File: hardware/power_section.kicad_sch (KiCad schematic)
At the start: 40 parts, among them J2 Conn_01x02, J3 USB_C_Receptacle_USB2.0_16P, U2 SW_SPDT_3pin, U3 HX3242, U4 TP4056, U5 FS8502A, U6 DW01A, U7 MIC5504-3.3YM5

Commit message: Second revision of schematic
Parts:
- removed U7: MIC5504-3.3YM5, Package_TO_SOT_SMD:SOT-23-5, symbol Regulator_Linear:MIC5504-3.3YM5
- added D4: 1N4148, Diode_THT:D_DO-35_SOD27_P7.62mm_Horizontal, symbol Diode:1N4148
- added R18: 1k, Resistor_SMD:R_0603_1608Metric, symbol Device:R
- added SW1: SW_Push, Button_Switch_SMD:SW_SPST_TL3342, symbol Switch:SW_Push
- added U7: AP2112K-3.3, Package_TO_SOT_SMD:SOT-23-5, symbol Regulator_Linear:AP2112K-3.3
- C3, C5: footprint Capacitor_THT:CP_Radial_D4.0mm_P1.50mm -> Capacitor_SMD:CP_Elec_6.3x3
- R10: renamed from R9; footprint (none) -> Resistor_SMD:R_0603_1608Metric
- R17: renamed from R16; value 0 -> 1k
- R20: renamed from R17; value 0 -> 1k
- R21: renamed from R18; value 1k -> 10k
- R9: renamed from R8; footprint (none) -> Resistor_SMD:R_0603_1608Metric
- renumbered R10 to R11, R11 to R12, R12 to R13, R13 to R14, R14 to R15, R15 to R16, R20 to R22, R21 to R23, R6 to R7, R7 to R8
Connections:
- net Ubatt is gone; now on net +BATT: R10.1, R9.2
- net +3V3: now also U7.5 (VOUT)
- net +5V: now also U7.1 (VIN)
- net +VSW: now also SW1.1
- net GND: now also U7.2 (GND)
- net POWER_EN: now also D4.2 (A); no longer R17.1, R20.2, R21.1
- net at D3.2 (A), L1.2, U3.1 (SW)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: now also U3.9 (SW)
- net at R20.1, R22.1: now also U7.3 (EN)
- new net: D4.1 (K), R17.1, R18.1, R20.2, R21.1
- new net: R18.2, SW1.2
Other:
- moved on the sheet: C11, R16, R17, R20, R21, R22, R23

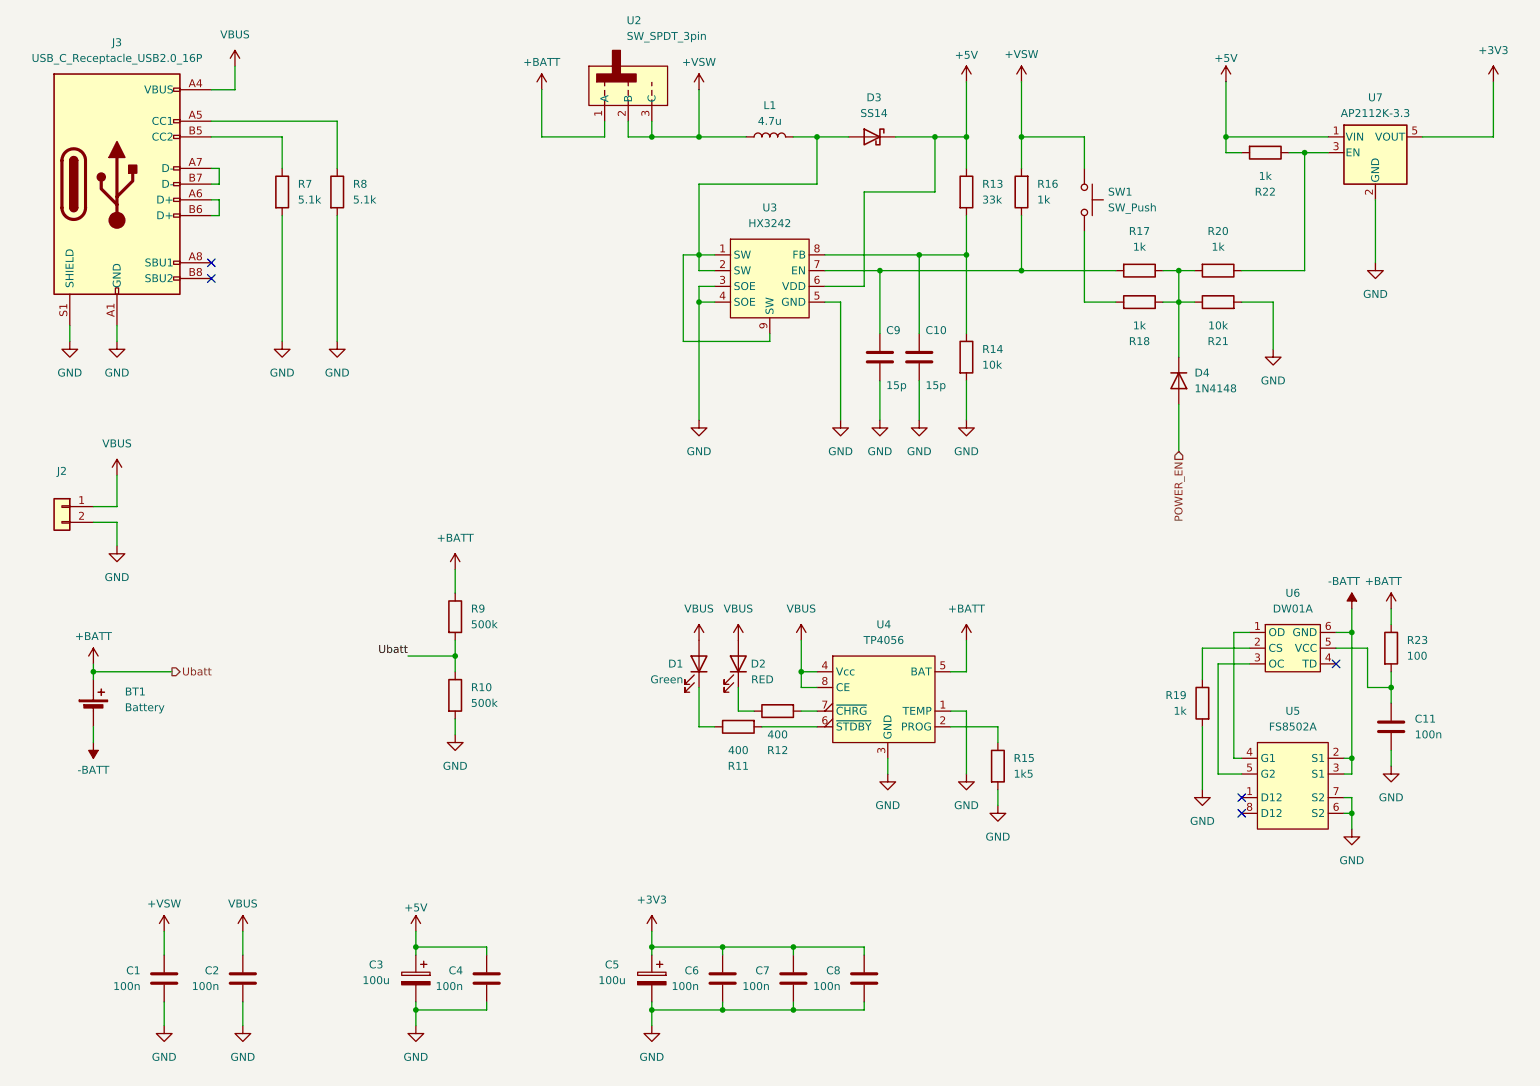
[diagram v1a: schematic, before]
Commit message: Initial PCB placement and some schematic changes
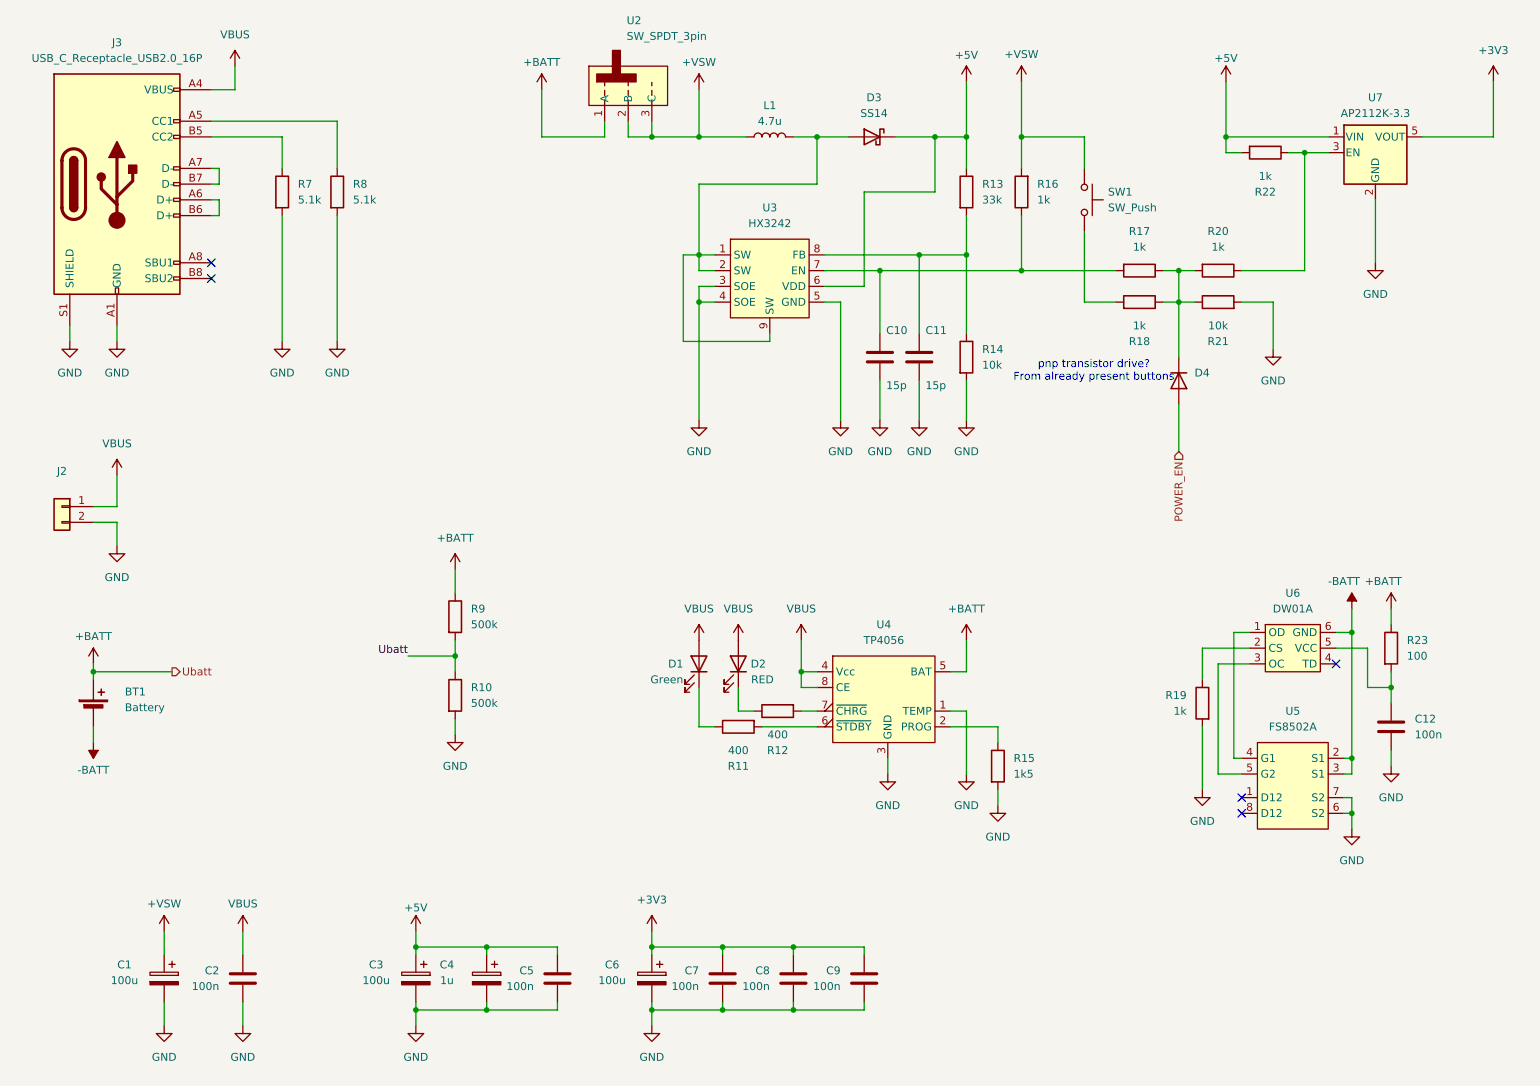
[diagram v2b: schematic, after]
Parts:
- removed C1: 100n, Capacitor_SMD:C_0603_1608Metric, symbol Device:C
- removed D4: 1N4148, Diode_THT:D_DO-35_SOD27_P7.62mm_Horizontal, symbol Diode:1N4148
- added C1: 100u, Capacitor_SMD:CP_Elec_6.3x3, symbol Device:C_Polarized
- added C4: 1u, Capacitor_SMD:CP_Elec_6.3x3, symbol Device:C_Polarized
- added D4: D, Diode_SMD:D_0805_2012Metric, symbol Device:D
- D1, D2: footprint Diode_SMD:D_0805_2012Metric -> Diode_SMD:D_0603_1608Metric_Pad1.05x0.95mm_HandSolder
- D3: footprint Diode_SMD:D_SMB -> Diode_SMD:D_SMA
- renumbered C9 to C10, C10 to C11, C11 to C12, C4 to C5, C5 to C6, C6 to C7, C7 to C8, C8 to C9
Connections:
- net +5V: now also C4.1
- net +VSW: now also C1.1
- net GND: now also C1.2, C4.2
- net POWER_EN: now also D4.2 (A)
- net at R17.1, R18.1, R20.2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: now also D4.1 (K)
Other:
- note added: "pnp transistor drive? From already present buttons"
- moved on the sheet: C5

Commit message: Audio improvements
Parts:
- removed C4: 1u, Capacitor_SMD:CP_Elec_6.3x3, symbol Device:C_Polarized
- renumbered C11 to C10, C12 to C11, C5 to C4, C6 to C5, C7 to C6, C8 to C7, C9 to C8, C10 to C9
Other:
- moved on the sheet: C4
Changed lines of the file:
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@@
 	)
 	(junction
-		(at 102.87 181.61)
-		(diameter 0)
-		(color 0 0 0 0)
-	)
-	(junction
 		(at 189.23 40.64)
 		(diameter 0)
@@
 	)
 	(junction
-		(at 102.87 171.45)
-		(diameter 0)
-		(color 0 0 0 0)
-	)
-	(junction
 		(at 39.37 127)
 		(diameter 0)
@@
 	(wire
 		(pts
-			(xy 102.87 180.34) (xy 102.87 181.61)
-		)
-		(stroke
-			(width 0)
-			(type default)
-		)
-	)
-	(wire
-		(pts
 			(xy 222.25 40.64) (xy 222.25 43.18)
 		)
@@
 	(wire
 		(pts
-			(xy 114.3 171.45) (xy 102.87 171.45)
-		)
-		(stroke
-			(width 0)
-			(type default)
-		)
-	)
-	(wire
-		(pts
 			(xy 156.21 48.26) (xy 156.21 40.64)
 		)
@@
 	(wire
 		(pts
-			(xy 114.3 180.34) (xy 114.3 181.61)
+			(xy 104.14 180.34) (xy 104.14 181.61)
 		)
 		(stroke
@@
 	(wire
 		(pts
-			(xy 114.3 181.61) (xy 102.87 181.61)
+			(xy 91.44 181.61) (xy 104.14 181.61)
 		)
 		(stroke
@@
 	(wire
 		(pts
-			(xy 102.87 171.45) (xy 91.44 171.45)
+			(xy 91.44 171.45) (xy 104.14 171.45)
 		)
 		(stroke
@@
 	(wire
 		(pts
-			(xy 102.87 171.45) (xy 102.87 172.72)
-		)
-		(stroke
-			(width 0)
-			(type default)
-		)
-	)
-	(wire
-		(pts
 			(xy 199.39 67.31) (xy 204.47 67.31)
 		)
@@
 	(wire
 		(pts
-			(xy 102.87 181.61) (xy 91.44 181.61)
-		)
-		(stroke
-			(width 0)
-			(type default)
-		)
-	)
-	(wire
-		(pts
 			(xy 147.32 135.89) (xy 156.21 135.89)
 		)
@@
 	(wire
 		(pts
-			(xy 114.3 172.72) (xy 114.3 171.45)
+			(xy 104.14 172.72) (xy 104.14 171.45)
 		)
 		(stroke
@@
 		(on_board yes)
 		(dnp no)
-		(property "Reference" "C6"
+		(property "Reference" "C5"
 			(at 123.1265 174.3075 0)
 			(effects
@@
 			(project "esp8266_pygame"
 				(path "/fc3c54fb-6d1c-4231-9293-8fcb9c0b9706/b1f9fade-b7ed-42bb-82ec-b3a822ff35a4"
-					(reference "C6")
+					(reference "C5")
 					(unit 1)
 				)
@@
 		(on_board yes)
 		(dnp no)
-		(property "Reference" "C11"
+		(property "Reference" "C10"
 			(at 173.736 71.882 0)
 			(effects
@@
 			(project "esp8266_pygame"
 				(path "/fc3c54fb-6d1c-4231-9293-8fcb9c0b9706/b1f9fade-b7ed-42bb-82ec-b3a822ff35a4"
-					(reference "C11")
+					(reference "C10")
 					(unit 1)
 				)
@@
 		(on_board yes)
 		(dnp no)
-		(property "Reference" "C7"
+		(property "Reference" "C6"
 			(at 137.16 175.26 0)
 			(effects
@@
 			(project "esp8266_pygame"
 				(path "/fc3c54fb-6d1c-4231-9293-8fcb9c0b9706/b1f9fade-b7ed-42bb-82ec-b3a822ff35a4"
-					(reference "C7")
+					(reference "C6")
 					(unit 1)
 				)
@@
 		(on_board yes)
 		(dnp no)
-		(property "Reference" "C9"
+		(property "Reference" "C8"
 			(at 160.02 175.26 0)
 			(effects
@@
 			(project "esp8266_pygame"
 				(path "/fc3c54fb-6d1c-4231-9293-8fcb9c0b9706/b1f9fade-b7ed-42bb-82ec-b3a822ff35a4"
-					(reference "C9")
+					(reference "C8")
 					(unit 1)
 				)
@@
 		(on_board yes)
 		(dnp no)
-		(property "Reference" "C10"
+		(property "Reference" "C9"
 			(at 167.386 71.882 0)
 			(effects
@@
 			(project "esp8266_pygame"
 				(path "/fc3c54fb-6d1c-4231-9293-8fcb9c0b9706/b1f9fade-b7ed-42bb-82ec-b3a822ff35a4"
-					(reference "C10")
+					(reference "C9")
 					(unit 1)
 				)
@@
 	)
 	(symbol
-		(lib_id "Device:C_Polarized")
-		(at 102.87 176.53 0)
-		(mirror y)
-		(unit 1)
-		(exclude_from_sim no)
-		(in_bom yes)
-		(on_board yes)
-		(dnp no)
-		(property "Reference" "C4"
-			(at 96.4565 174.3075 0)
-			(effects
-				(font
-					(size 1.27 1.27)
-				)
-			)
-		)
-		(property "Value" "1u"
-			(at 96.4565 176.8475 0)
-			(effects
-				(font
-					(size 1.27 1.27)
-				)
-			)
-		)
-		(property "Footprint" "Capacitor_SMD:CP_Elec_6.3x3"
-			(at 101.9048 180.34 0)
-			(effects
-				(font
-					(size 1.27 1.27)
-				)
-				(hide yes)
-			)
-		)
-		(property "Datasheet" "~"
-			(at 102.87 176.53 0)
-			(effects
-				(font
-					(size 1.27 1.27)
-				)
-				(hide yes)
-			)
-		)
-		(property "Description" ""
-			(at 102.87 176.53 0)
-			(effects
-				(font
-					(size 1.27 1.27)
-				)
-			)
-		)
-		(pin "1"
-		)
-		(pin "2"
-		)
-		(instances
-			(project "esp8266_pygame"
-				(path "/fc3c54fb-6d1c-4231-9293-8fcb9c0b9706/b1f9fade-b7ed-42bb-82ec-b3a822ff35a4"
-					(reference "C4")
-					(unit 1)
-				)
-			)
-		)
-	)
-	(symbol
 		(lib_id "power:+BATT")
 		(at 111.76 33.02 0)
@@
 		(dnp no)
 		(fields_autoplaced yes)
-		(property "Reference" "C12"
+		(property "Reference" "C11"
 			(at 252.73 134.62 0)
 			(effects
@@
 			(project "esp8266_pygame"
 				(path "/fc3c54fb-6d1c-4231-9293-8fcb9c0b9706/b1f9fade-b7ed-42bb-82ec-b3a822ff35a4"
-					(reference "C12")
+					(reference "C11")
 					(unit 1)
 				)
@@
 		(on_board yes)
 		(dnp no)
-		(property "Reference" "C8"
+		(property "Reference" "C7"
 			(at 148.59 175.26 0)
 			(effects
@@
 			(project "esp8266_pygame"
 				(path "/fc3c54fb-6d1c-4231-9293-8fcb9c0b9706/b1f9fade-b7ed-42bb-82ec-b3a822ff35a4"
-					(reference "C8")
+					(reference "C7")
 					(unit 1)
 				)
@@
 	(symbol
 		(lib_id "Device:C")
-		(at 114.3 176.53 0)
+		(at 104.14 176.53 0)
 		(mirror x)
 		(unit 1)
@@
 		(on_board yes)
 		(dnp no)
-		(property "Reference" "C5"
-			(at 110.49 175.26 0)
+		(property "Reference" "C4"
+			(at 100.33 175.26 0)
 			(effects
 				(font
@@
 		)
 		(property "Value" "100n"
-			(at 110.49 177.8 0)
+			(at 100.33 177.8 0)
 			(effects
 				(font
@@
 		)
 		(property "Footprint" "Capacitor_SMD:C_0603_1608Metric"
-			(at 115.2652 172.72 0)
+			(at 105.1052 172.72 0)
 			(effects
 				(font
@@
 		)
 		(property "Datasheet" "~"
-			(at 114.3 176.53 0)
+			(at 104.14 176.53 0)
 			(effects
 				(font
@@
 		)
 		(property "Description" ""
-			(at 114.3 176.53 0)
+			(at 104.14 176.53 0)
 			(effects
 				(font
@@
 			(project "esp8266_pygame"
 				(path "/fc3c54fb-6d1c-4231-9293-8fcb9c0b9706/b1f9fade-b7ed-42bb-82ec-b3a822ff35a4"
-					(reference "C5")
+					(reference "C4")
 					(unit 1)
 				)

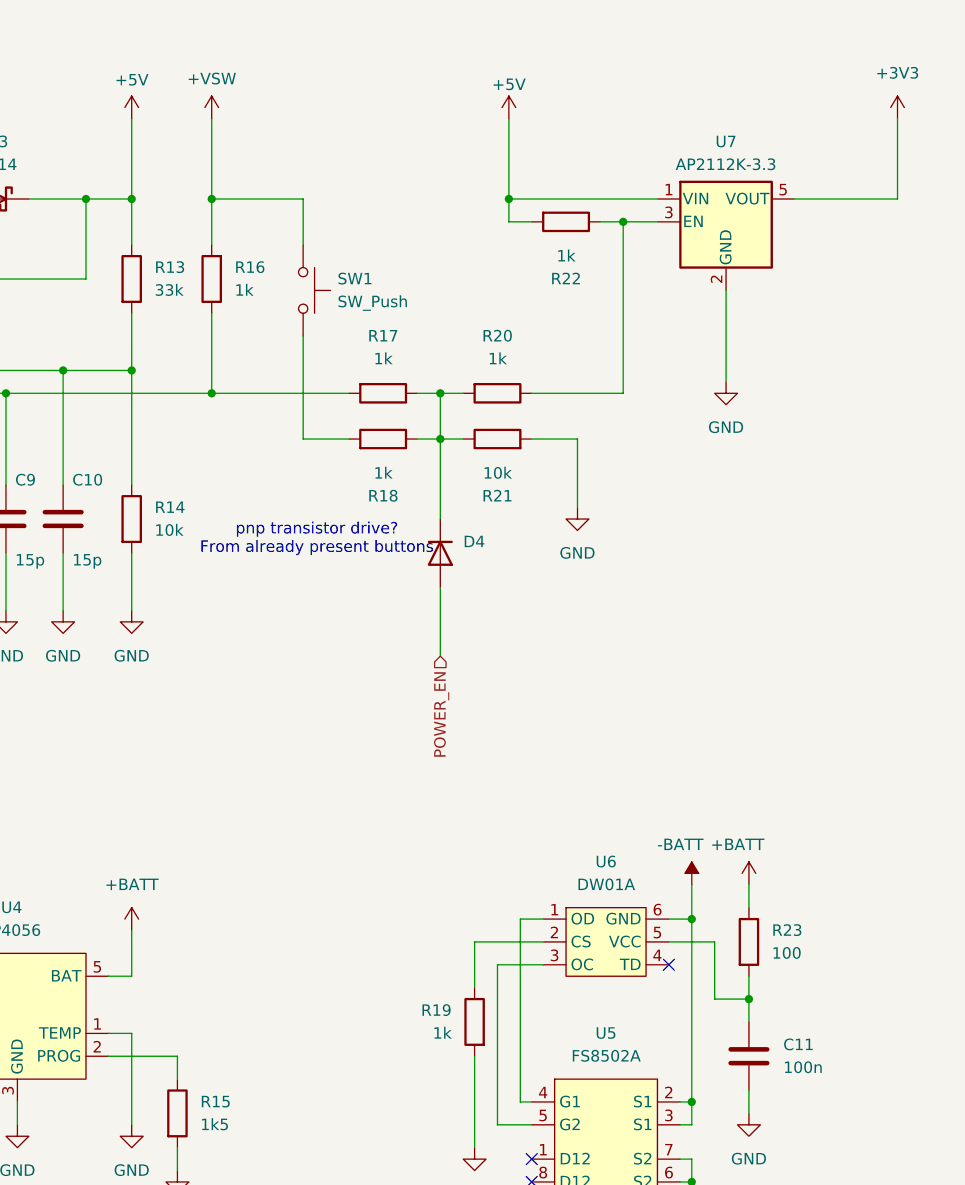
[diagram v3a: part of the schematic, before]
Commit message: Fixed power enable bypass
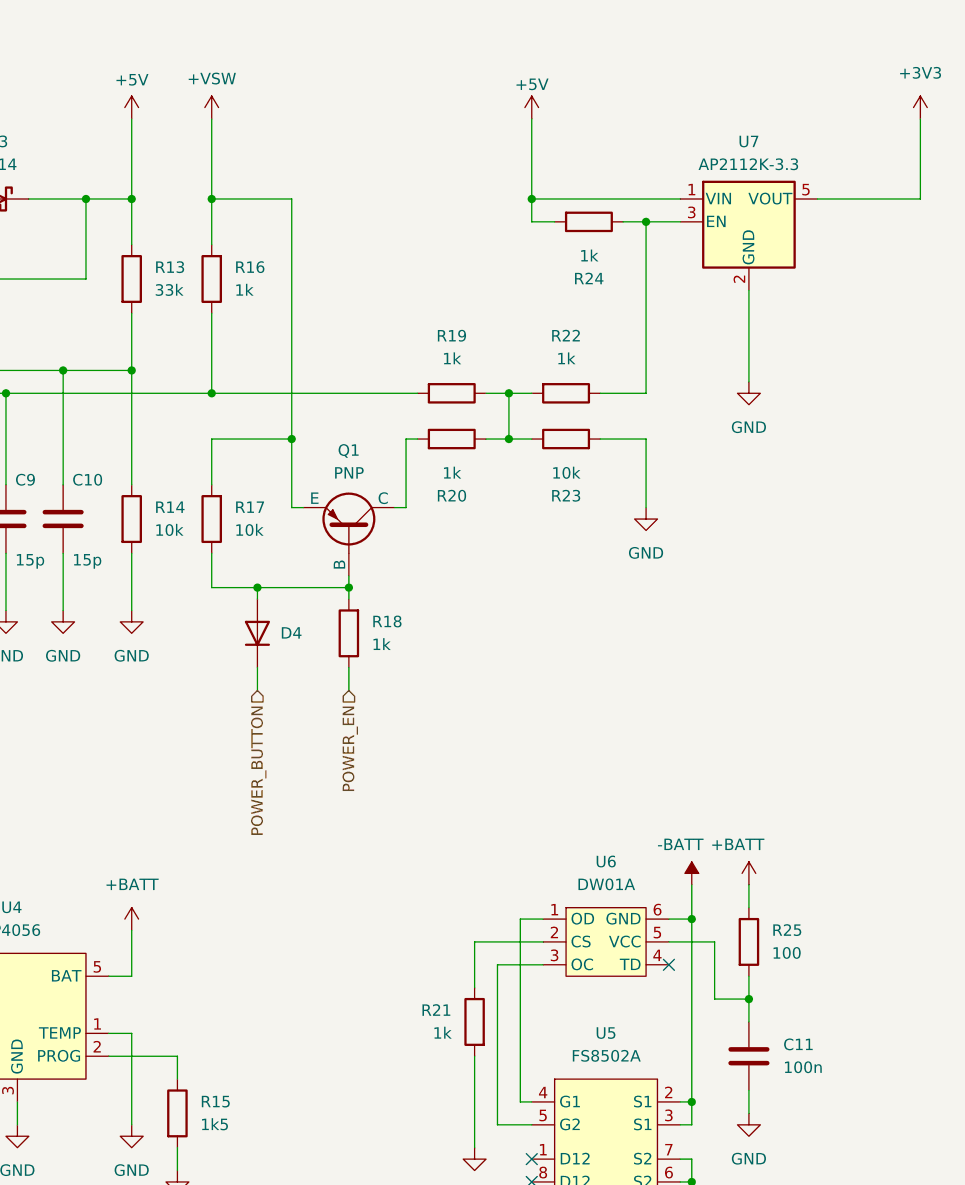
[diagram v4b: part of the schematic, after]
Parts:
- removed SW1: SW_Push, Button_Switch_SMD:SW_SPST_TL3342, symbol Switch:SW_Push
- added Q1: PNP, Package_TO_SOT_SMD:SOT-23, symbol Simulation_SPICE:PNP
- added R17: 10k, Resistor_SMD:R_0603_1608Metric, symbol Device:R
- added R18: 1k, Resistor_SMD:R_0603_1608Metric, symbol Device:R
- renumbered R17 to R19, R18 to R20, R19 to R21, R20 to R22, R21 to R23, R22 to R24, R23 to R25
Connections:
- net +VSW: now also Q1.3 (E), R17.2
- net POWER_EN: now also R18.1; no longer D4.2 (A)
- net at R19.1, R20.1, R22.2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: no longer D4.1 (K)
- net at R20.2: now also Q1.1 (C)
- new net: D4.2 (A), Q1.2 (B), R17.1, R18.2
- new net POWER_BUTTON: D4.1 (K)
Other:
- note removed: "pnp transistor drive? From already present buttons"
- moved on the sheet: D4, R19, R20, R22, R23, R24, U7

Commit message: Add PCB edges marks
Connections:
- net +BATT: no longer R10.1, R9.2
- new net Ubatt: R10.1, R9.2
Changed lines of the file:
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@@
-	)
-	(junction
-		(at 39.37 127)
-		(diameter 0)
-		(color 0 0 0 0)
 	)
 	(junction
@@
 	(wire
 		(pts
-			(xy 39.37 125.73) (xy 39.37 127)
-		)
-		(stroke
-			(width 0)
-			(type default)
-		)
-	)
-	(wire
-		(pts
 			(xy 177.8 135.89) (xy 185.42 135.89)
 		)
@@
 	(wire
 		(pts
-			(xy 39.37 127) (xy 52.07 127)
-		)
-		(stroke
-			(width 0)
-			(type default)
-		)
-	)
-	(wire
-		(pts
 			(xy 218.44 135.89) (xy 218.44 146.05)
 		)
@@
 	(wire
 		(pts
-			(xy 39.37 127) (xy 39.37 128.27)
+			(xy 39.37 125.73) (xy 39.37 128.27)
 		)
 		(stroke
@@
 			(width 0)
 			(type default)
-		)
-	)
-	(label "Ubatt"
-		(at 90.17 124.46 180)
-		(effects
-			(font
-				(size 1.27 1.27)
-			)
-			(justify right bottom)
 		)
 	)
@@
 	(hierarchical_label "Ubatt"
 		(shape output)
-		(at 52.07 127 0)
+		(at 90.17 124.46 180)
 		(effects
 			(font
 				(size 1.27 1.27)
 			)
-			(justify left)
-		)
-	)
+			(justify right)
+		)
+	)
